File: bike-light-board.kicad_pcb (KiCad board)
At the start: 4 copper layers, 40.2 x 69 mm, 107 parts, among them J1 KH-TYPE-C-16P, J2 S2B-PH-SM4-TB, P2 WirePad, P3 WirePad, Q1 HX2301A, Q2 L2N7002DW1T1G, Q3 HX2301A, Q4 SMD0805-20, Q5 HX2301A, SW1 SW_Push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

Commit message: update flash chip to faster version
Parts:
- removed G*** (x2): LOGO, bike-light-board:Logo_Lil_Light
- R28: value 47k -> 10k
- R29: value 47k -> 5k1
- U4: value P25Q40H-SSH-IT -> XT25F32BSOIG

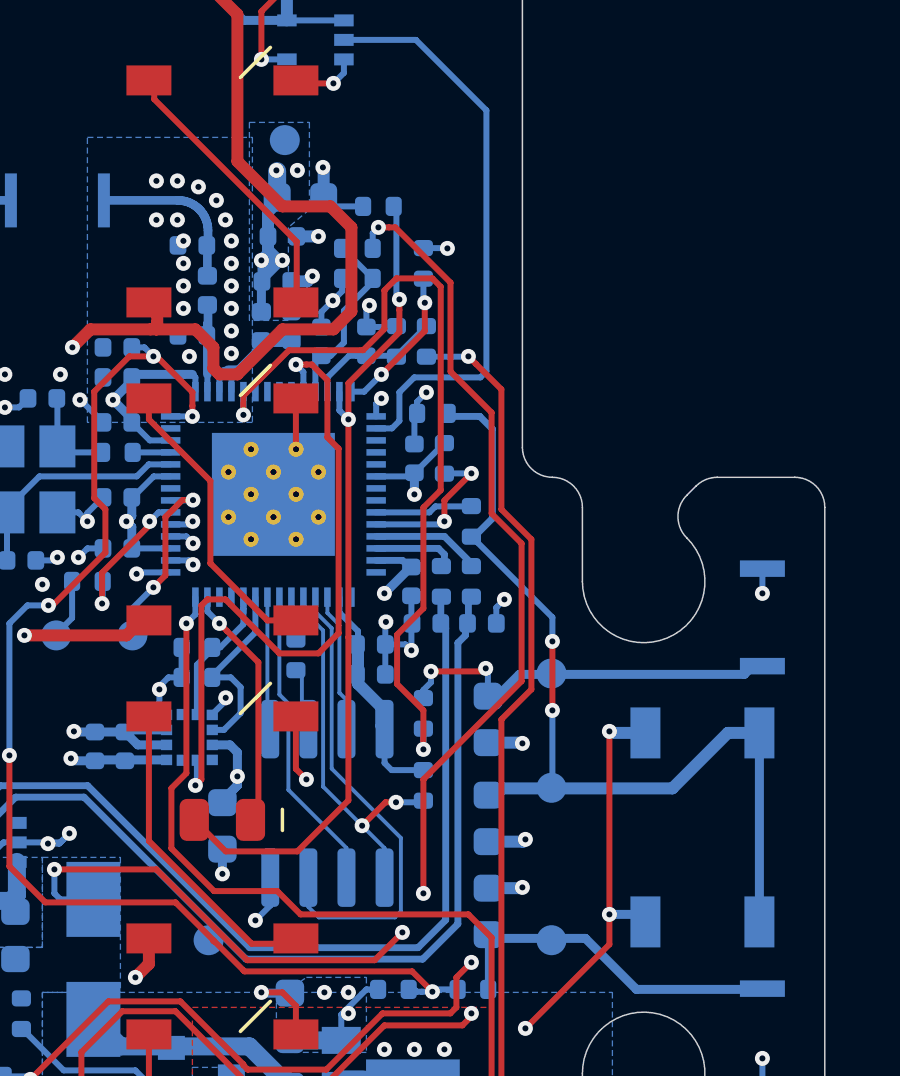
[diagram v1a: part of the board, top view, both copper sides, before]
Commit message: add 10k to IO0 pin to fix boot issue
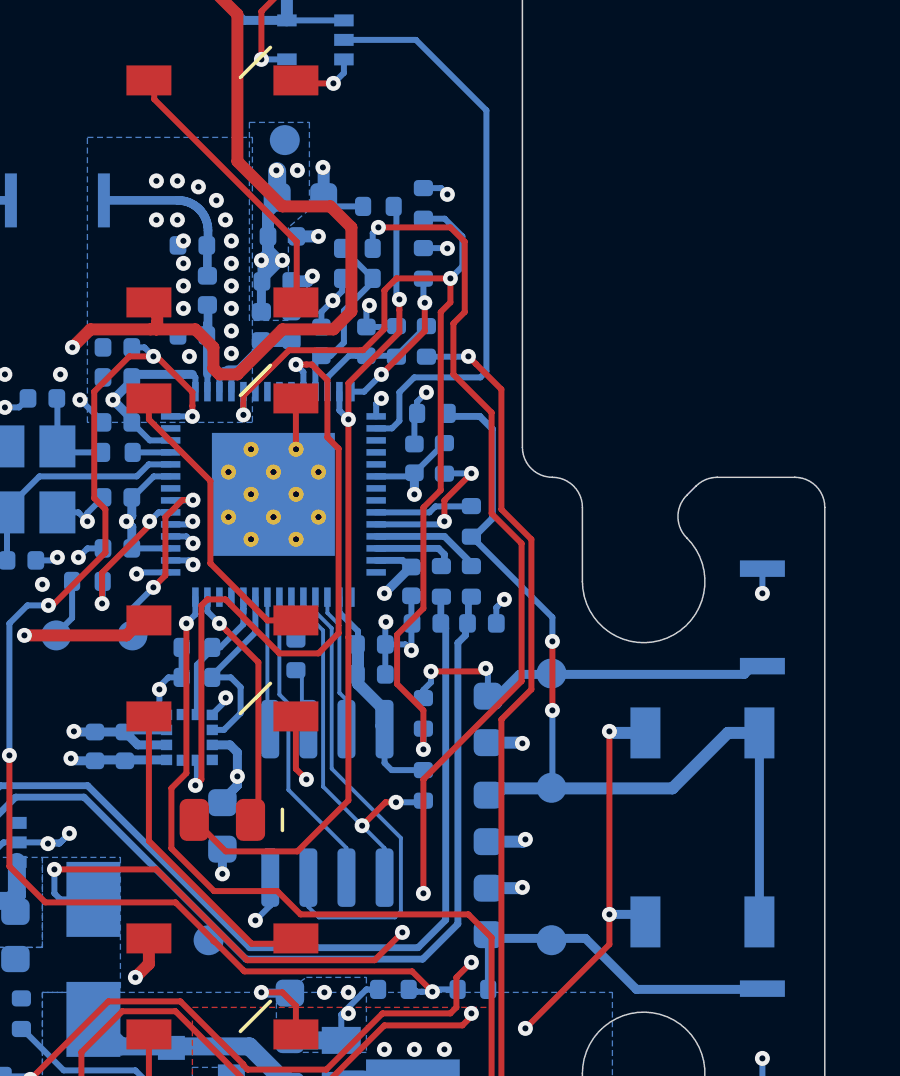
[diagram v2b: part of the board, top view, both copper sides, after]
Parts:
- added R21: 10k, Resistor_SMD:R_0402_1005Metric, B.Cu at (167.7, 82.9)
- SW1: value SW_Push -> TS5220A
- SW2, SW3: value STO-060A16AB -> DNP
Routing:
- net IO0: track 27.6 -> 31.3 mm, vias 2 -> 3
- net /VBUS: track 45.4 -> 46.8 mm
- net +3V3: track 59.4 -> 60.3 mm, vias 18 -> 19
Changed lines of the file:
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@@
     (thickness 1.6)
     (drawings 58)
-    (tracks 942)
+    (tracks 952)
     (zones 0)
-    (modules 105)
+    (modules 106)
     (nets 87)
   )
@@
     (42 Eco1.User user hide)
     (43 Eco2.User user hide)
-    (44 Edge.Cuts user)
+    (44 Edge.Cuts user hide)
     (45 Margin user hide)
     (46 B.CrtYd user hide)
@@
     (add_net USB_D-)
   )
+  (module Resistor_SMD:R_0402_1005Metric (layer B.Cu)
+    (at 167.7 82.87 90)
+    (descr "Resistor SMD 0402 (1005 Metric), square (rectangular) end terminal, IPC_7351 nominal, (Body size source: IPC-SM-782 page 72, https://www.pcb-3d.com/wordpress/wp-content/uploads/ipc-sm-782a_amendment_1_and_2.pdf), generated with kicad-footprint-generator")
+    (tags resistor)
+    (attr smd)
+    (fp_text reference R21 (at 0 1.17 90) (layer B.SilkS) hide
+      (effects (font (size 1 1) (thickness 0.15)) (justify mirror))
+    )
+    (fp_text value 10k (at 0 -1.17 90) (layer B.Fab)
+      (effects (font (size 1 1) (thickness 0.15)) (justify mirror))
+    )
+    (fp_text user %R (at 0 0 90) (layer B.Fab)
+      (effects (font (size 0.26 0.26) (thickness 0.04)) (justify mirror))
+    )
+    (fp_line (start 0.93 -0.47) (end -0.93 -0.47) (layer B.CrtYd) (width 0.05))
+    (fp_line (start 0.93 0.47) (end 0.93 -0.47) (layer B.CrtYd) (width 0.05))
+    (fp_line (start -0.93 0.47) (end 0.93 0.47) (layer B.CrtYd) (width 0.05))
+    (fp_line (start -0.93 -0.47) (end -0.93 0.47) (layer B.CrtYd) (width 0.05))
+    (fp_line (start -0.153641 -0.38) (end 0.153641 -0.38) (layer B.SilkS) (width 0.12))
+    (fp_line (start -0.153641 0.38) (end 0.153641 0.38) (layer B.SilkS) (width 0.12))
+    (fp_line (start 0.525 -0.27) (end -0.525 -0.27) (layer B.Fab) (width 0.1))
+    (fp_line (start 0.525 0.27) (end 0.525 -0.27) (layer B.Fab) (width 0.1))
+    (fp_line (start -0.525 0.27) (end 0.525 0.27) (layer B.Fab) (width 0.1))
+    (fp_line (start -0.525 -0.27) (end -0.525 0.27) (layer B.Fab) (width 0.1))
+    (pad 2 smd roundrect (at 0.51 0 90) (size 0.54 0.64) (layers B.Cu B.Paste B.Mask) (roundrect_rratio 0.25)
+      (net 2 +3V3))
+    (pad 1 smd roundrect (at -0.51 0 90) (size 0.54 0.64) (layers B.Cu B.Paste B.Mask) (roundrect_rratio 0.25)
+      (net 57 IO0))
+    (model ${KISYS3DMOD}/Resistor_SMD.3dshapes/R_0402_1005Metric.wrl
+      (at (xyz 0 0 0))
+      (scale (xyz 1 1 1))
+      (rotate (xyz 0 0 0))
+    )
+  )
   (module footprints:ICT_TestPoint_Pad_D1.00mm (layer B.Cu)
     (at 171.97 98.54)
@@
       (effects (font (size 0.8 0.8) (thickness 0.15)) (justify mirror))
     )
-    (fp_text value STO-060A16AB (at 0 -2.5 90) (layer B.Fab) hide
+    (fp_text value DNP (at 0 -2.5 90) (layer B.Fab) hide
       (effects (font (size 1 1) (thickness 0.15)) (justify mirror))
     )
@@
       (effects (font (size 0.8 0.8) (thickness 0.15)) (justify mirror))
     )
-    (fp_text value STO-060A16AB (at 0 -2.5 90) (layer B.Fab) hide
+    (fp_text value DNP (at 0 -2.5 90) (layer B.Fab) hide
       (effects (font (size 1 1) (thickness 0.15)) (justify mirror))
     )
@@
       (effects (font (size 0.8 0.8) (thickness 0.15)) (justify mirror))
     )
-    (fp_text value SW_Push (at 0 -3.75 90) (layer B.Fab) hide
+    (fp_text value TS5220A (at 0 -3.75 90) (layer B.Fab) hide
       (effects (font (size 1 1) (thickness 0.15)) (justify mirror))
     )
@@
   (segment (start 173.9 106.57) (end 173.9 100.470002) (width 0.2) (layer F.Cu) (net 2))
   (segment (start 175.099999 100.520508) (end 173.950506 100.520508) (width 0.4) (layer B.Cu) (net 2))
+  (via (at 168.5 82.57) (size 0.5) (drill 0.2) (layers F.Cu B.Cu) (net 2))
+  (segment (start 167.7 82.36) (end 168.29 82.36) (width 0.2) (layer B.Cu) (net 2))
+  (segment (start 168.29 82.36) (end 168.5 82.57) (width 0.2) (layer B.Cu) (net 2))
   (segment (start 163.15 75.59) (end 163.22 75.52) (width 0.4) (layer B.Cu) (net 3))
   (segment (start 163.15 76.77) (end 163.15 75.59) (width 0.4) (layer B.Cu) (net 3))
@@
   (segment (start 167 106.57) (end 167.7 105.87) (width 0.2) (layer In1.Cu) (net 46))
   (segment (start 167 107.17) (end 167 106.57) (width 0.2) (layer In1.Cu) (net 46))
-  (segment (start 167.7 105.87) (end 167.7 102.07) (width 0.2) (layer F.Cu) (net 46))
-  (segment (start 168.604011 85.51155) (end 166.762461 83.67) (width 0.2) (layer F.Cu) (net 46))
-  (segment (start 169.972989 89.842989) (end 168.604011 88.474011) (width 0.2) (layer F.Cu) (net 46))
-  (segment (start 170.972989 98.797011) (end 170.972989 94.205451) (width 0.2) (layer F.Cu) (net 46))
-  (segment (start 169.972989 93.205452) (end 169.972989 89.842989) (width 0.2) (layer F.Cu) (net 46))
-  (segment (start 166.553553 83.67) (end 166.2 83.67) (width 0.2) (layer F.Cu) (net 46))
-  (segment (start 167.7 102.07) (end 170.972989 98.797011) (width 0.2) (layer F.Cu) (net 46))
-  (segment (start 168.604011 88.474011) (end 168.604011 85.51155) (width 0.2) (layer F.Cu) (net 46))
-  (segment (start 170.972989 94.205451) (end 169.972989 93.205452) (width 0.2) (layer F.Cu) (net 46))
-  (segment (start 166.762461 83.67) (end 166.553553 83.67) (width 0.2) (layer F.Cu) (net 46))
+  (segment (start 170.972989 98.797011) (end 167.7 102.07) (width 0.2) (layer F.Cu) (net 46))
+  (segment (start 168.7 88.57) (end 169.972989 89.842989) (width 0.2) (layer F.Cu) (net 46))
+  (segment (start 167.7 102.07) (end 167.7 105.87) (width 0.2) (layer F.Cu) (net 46))
+  (segment (start 170.972989 94.205451) (end 170.972989 98.797011) (width 0.2) (layer F.Cu) (net 46))
+  (segment (start 169.972989 89.842989) (end 169.972989 93.205452) (width 0.2) (layer F.Cu) (net 46))
+  (segment (start 168.7 86.87) (end 168.7 88.57) (width 0.2) (layer F.Cu) (net 46))
+  (segment (start 169.077001 86.492999) (end 168.7 86.87) (width 0.2) (layer F.Cu) (net 46))
+  (segment (start 169.077001 84.147001) (end 169.077001 86.492999) (width 0.2) (layer F.Cu) (net 46))
+  (segment (start 168.6 83.67) (end 169.077001 84.147001) (width 0.2) (layer F.Cu) (net 46))
+  (segment (start 169.972989 93.205452) (end 170.972989 94.205451) (width 0.2) (layer F.Cu) (net 46))
+  (segment (start 166.2 83.67) (end 168.6 83.67) (width 0.2) (layer F.Cu) (net 46))
   (segment (start 165.49 87.95) (end 165.8 87.95) (width 0.2) (layer B.Cu) (net 47))
   (segment (start 165.22 87.95) (end 165.49 87.95) (width 0.2) (layer B.Cu) (net 47))
@@
   (via (at 167.7 101.07) (size 0.5) (drill 0.2) (layers F.Cu B.Cu) (net 57))
   (segment (start 167.7 100.38) (end 167.7 101.07) (width 0.2) (layer B.Cu) (net 57))
+  (segment (start 167.7 83.38) (end 168.41 83.38) (width 0.2) (layer B.Cu) (net 57))
+  (segment (start 168.41 83.38) (end 169 83.97) (width 0.2) (layer B.Cu) (net 57))
+  (segment (start 169 83.97) (end 169 84.97) (width 0.2) (layer B.Cu) (net 57))
+  (via (at 168.6 85.37) (size 0.5) (drill 0.2) (layers F.Cu B.Cu) (net 57))
+  (segment (start 169 84.97) (end 168.6 85.37) (width 0.2) (layer B.Cu) (net 57))
   (segment (start 167.7 99.77) (end 167.7 101.07) (width 0.2) (layer F.Cu) (net 57))
   (segment (start 166.822999 98.892999) (end 167.7 99.77) (width 0.2) (layer F.Cu) (net 57))
+  (segment (start 166.822999 97.247001) (end 166.822999 98.892999) (width 0.2) (layer F.Cu) (net 57))
   (segment (start 167.7 96.37) (end 166.822999 97.247001) (width 0.2) (layer F.Cu) (net 57))
-  (segment (start 168 85.37) (end 168.277001 85.647001) (width 0.2) (layer F.Cu) (net 57))
-  (segment (start 168.277001 92.430539) (end 167.7 93.00754) (width 0.2) (layer F.Cu) (net 57))
-  (segment (start 168.277001 85.647001) (end 168.277001 92.430539) (width 0.2) (layer F.Cu) (net 57))
   (segment (start 167.7 93.00754) (end 167.7 96.37) (width 0.2) (layer F.Cu) (net 57))
-  (segment (start 166.822999 97.247001) (end 166.822999 98.892999) (width 0.2) (layer F.Cu) (net 57))
-  (segment (start 166.8 85.37) (end 168 85.37) (width 0.2) (layer F.Cu) (net 57))
+  (segment (start 168.277001 92.430539) (end 167.7 93.00754) (width 0.2) (layer F.Cu) (net 57))
+  (segment (start 168.277001 92.430539) (end 168.277001 86.492999) (width 0.2) (layer F.Cu) (net 57))
+  (segment (start 168.6 86.17) (end 168.6 85.37) (width 0.2) (layer F.Cu) (net 57))
+  (segment (start 168.277001 86.492999) (end 168.6 86.17) (width 0.2) (layer F.Cu) (net 57))
+  (segment (start 166.8 85.37) (end 168.6 85.37) (width 0.2) (layer F.Cu) (net 57))
   (segment (start 166.4 85.77) (end 166.8 85.37) (width 0.2) (layer F.Cu) (net 57))
   (segment (start 166.4 87.055998) (end 166.4 85.77) (width 0.2) (layer F.Cu) (net 57))
